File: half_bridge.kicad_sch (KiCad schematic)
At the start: 31 parts, among them Q1 IGC019S06S1XTMA1, Q2 IGC019S06S1XTMA1, U19 NCS2220AMUT1G, U4 ACS37030LLZATR-065B3, U5 LMG1205YFXR

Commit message: wip gate driver change
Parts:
- removed C21: 0402B104K6R3CT, Capacitor_SMD:C_0402_1005Metric, symbol Device:C
- removed R13, R18: ~, Resistor_SMD:R_0402_1005Metric_Pad0.72x0.64mm_HandSolder, symbol Device:R
- removed R47: CSR0402FKR500, Resistor_SMD:R_0402_1005Metric, symbol Device:R
- removed U5: LMG1205YFXR, NanoGaN:BGA12C40P4X4_173X188X68, symbol NanoGaN:LMG1205YFXR
- added C31: 0402B104K6R3CT, Capacitor_SMD:C_0402_1005Metric, symbol Device:C
- added D7: MBR2H200SF, Diode_SMD:D_SOD-123F, symbol Device:D
- added R45: 0402WGF4702TCE, Resistor_SMD:R_0402_1005Metric, symbol Device:R
- added U11, U5: 1EDN7136U, NanoGaN:1EDN71X6U, symbol NanoGaN:1EDN7116U
- C22: value 0402B104K6R3CT -> CL05B105KQ5NQNC; Capacitance 100n -> 1u; LCSC C424821 -> C307427
- R44: value CSR0402FKR500 -> 0402WGF4702TCE; LCSC C346785 -> C25792; Resistance 0R5 -> 47k
- R8, R9: value CRCW04021R00FKEDHP -> 0402WGF4702TCE; LCSC C2077491 -> C25792; Resistance 1 -> 47k
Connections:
- net HOH is gone; now on net GATE+: R8.1
- net HOL is gone; now on net GATE-: R44.1
- net LOH is gone; now on net GATE-: R9.1
- net +5V: now also U11.1 (VDD); no longer C22.1
- net GATE+: now also R45.1
- net GND: now also U11.4 (VSS); no longer C22.2
- net HIGH_GATE: now also U5.6 (OUT_SNK), U5.7 (OUT_SRC); no longer R44.2, R8.2
- net HS: now also C22.1, C31.1, U5.4 (VSS)
- net LOW_GATE: now also U11.6 (OUT_SNK), U11.7 (OUT_SRC); no longer R9.2
- new net: C22.2, C31.2, D7.1 (K)
- new net BST: D7.2 (A), U11.5 (BST), U5.1 (VDD)
- new net H+: R8.2, U5.2 (IN+)
- new net H-: R9.2, U5.3 (IN-)
- new net L+: R44.2, U11.2 (IN+)
- new net L-: R45.2, U11.3 (IN-)
- no-connect marks 0 -> 1
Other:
- note added: "Halfbridge and GateDrivers"
- note added: "U_DC High Frequency Decoupling Capacitors"
- note removed: "Gate Driver"
- note removed: "Halfbridge"
- note removed: "Q_g = 13nC Q_rr = 0 nC CBST > 5-6 nF"
- moved on the sheet: C15, C16, C20, C24, C25, C28, C36, C44, C46, C47, Q1, Q2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

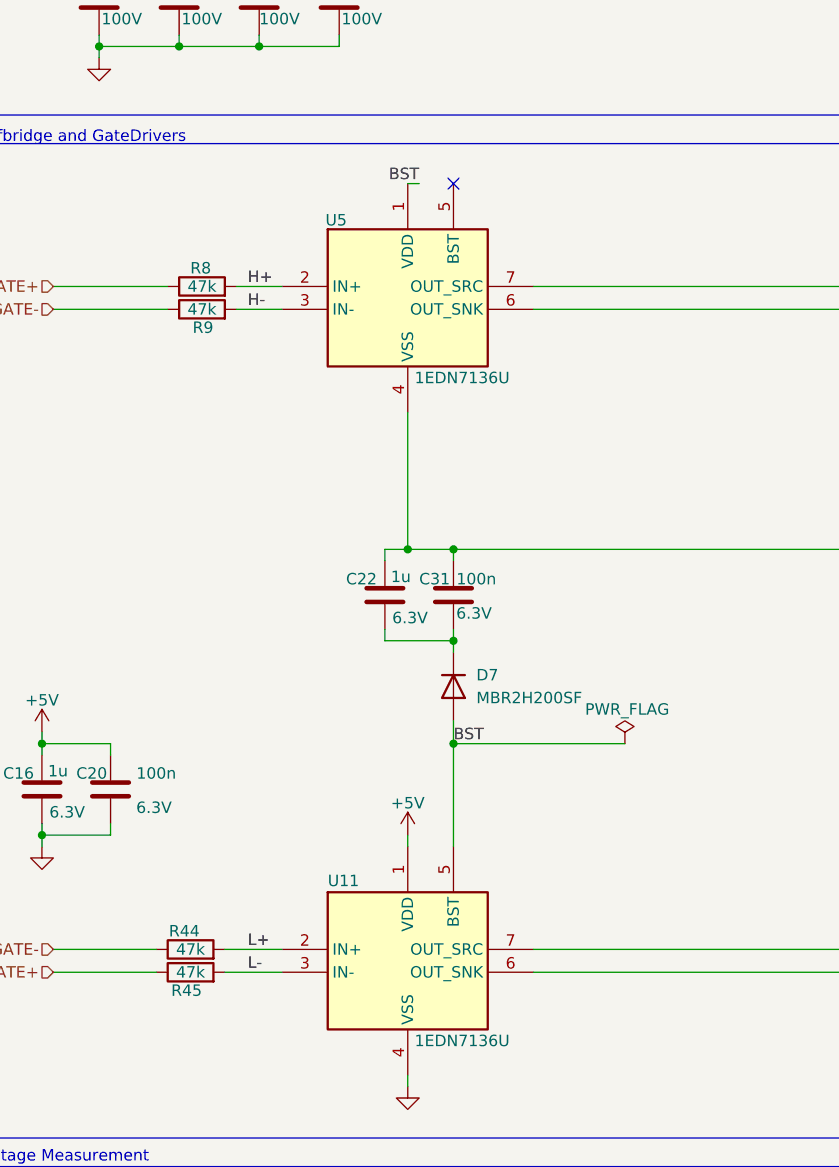
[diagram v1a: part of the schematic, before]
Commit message: gate driver change is complete
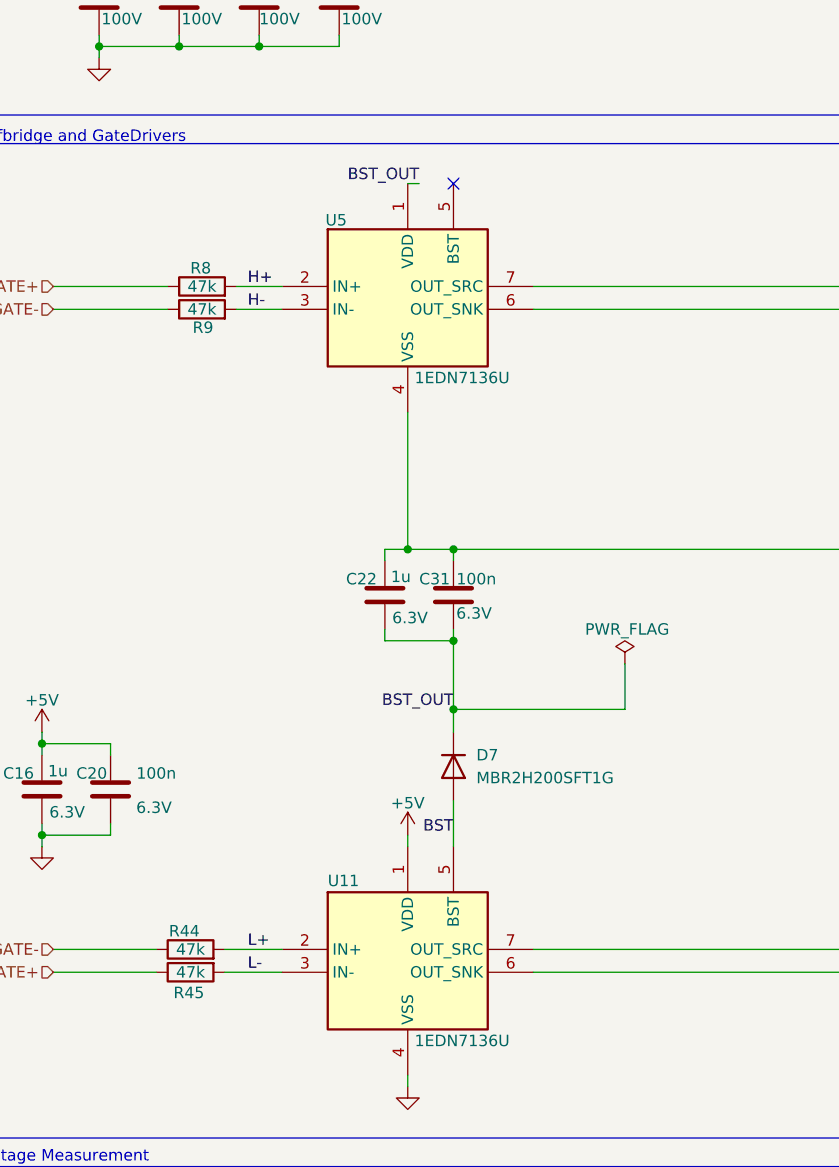
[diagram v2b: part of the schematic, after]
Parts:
- D7: value MBR2H200SF -> MBR2H200SFT1G
- R10: value 0603WAF3902T5E -> NQ02WGF3902TCE; footprint Resistor_SMD:R_0603_1608Metric -> Resistor_SMD:R_0402_1005Metric; LCSC C23153 -> C965259
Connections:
- net BST: no longer U5.1 (VDD)
- net BST_OUT: now reaches C22.2, C31.2, D7.1 (K)
- net BST_OUT: now also U5.1 (VDD)
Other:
- moved on the sheet: D7
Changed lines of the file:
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@@
 	)
 	(junction
-		(at 66.04 111.76)
-		(diameter 0)
-		(color 0 0 0 0)
-	)
-	(junction
 		(at 123.19 90.17)
 		(diameter 0)
@@
 	)
 	(junction
+		(at 66.04 107.95)
+		(diameter 0)
+		(color 0 0 0 0)
+	)
+	(junction
 		(at 20.32 111.76)
 		(diameter 0)
@@
 	)
 	(junction
+		(at 66.04 100.33)
+		(diameter 0)
+		(color 0 0 0 0)
+	)
+	(junction
 		(at 110.49 134.62)
 		(diameter 0)
@@
 	)
 	(junction
-		(at 66.04 100.33)
-		(diameter 0)
-		(color 0 0 0 0)
-	)
-	(junction
 		(at 146.05 96.52)
 		(diameter 0)
@@
 	(wire
 		(pts
-			(xy 66.04 100.33) (xy 66.04 101.6)
+			(xy 60.96 90.17) (xy 60.96 74.93)
 		)
 		(stroke
@@
 	(wire
 		(pts
-			(xy 60.96 90.17) (xy 60.96 74.93)
+			(xy 20.32 111.76) (xy 27.94 111.76)
 		)
 		(stroke
@@
 	(wire
 		(pts
-			(xy 20.32 111.76) (xy 27.94 111.76)
+			(xy 66.04 90.17) (xy 66.04 91.44)
 		)
 		(stroke
@@
 	(wire
 		(pts
-			(xy 66.04 90.17) (xy 66.04 91.44)
+			(xy 58.42 100.33) (xy 66.04 100.33)
 		)
 		(stroke
@@
 	(wire
 		(pts
-			(xy 66.04 111.76) (xy 66.04 123.19)
-		)
-		(stroke
-			(width 0)
-			(type default)
-		)
-	)
-	(wire
-		(pts
 			(xy 243.84 118.11) (xy 237.49 118.11)
 		)
@@
 	(wire
 		(pts
-			(xy 66.04 109.22) (xy 66.04 111.76)
-		)
-		(stroke
-			(width 0)
-			(type default)
-		)
-	)
-	(wire
-		(pts
 			(xy 60.96 49.53) (xy 62.23 49.53)
 		)
@@
 	(wire
 		(pts
+			(xy 85.09 107.95) (xy 85.09 102.87)
+		)
+		(stroke
+			(width 0)
+			(type default)
+		)
+	)
+	(wire
+		(pts
 			(xy 152.4 129.54) (xy 153.67 129.54)
 		)
@@
 	(wire
 		(pts
-			(xy 21.59 137.16) (xy 33.02 137.16)
-		)
-		(stroke
-			(width 0)
-			(type default)
-		)
-	)
-	(wire
-		(pts
-			(xy 66.04 100.33) (xy 58.42 100.33)
-		)
-		(stroke
-			(width 0)
-			(type default)
-		)
-	)
-	(wire
-		(pts
 			(xy 19.05 187.96) (xy 19.05 189.23)
 		)
@@
 	(wire
 		(pts
+			(xy 66.04 100.33) (xy 66.04 107.95)
+		)
+		(stroke
+			(width 0)
+			(type default)
+		)
+	)
+	(wire
+		(pts
 			(xy 227.33 96.52) (xy 227.33 106.68)
 		)
@@
 	(wire
 		(pts
+			(xy 66.04 118.11) (xy 66.04 123.19)
+		)
+		(stroke
+			(width 0)
+			(type default)
+		)
+	)
+	(wire
+		(pts
 			(xy 227.33 96.52) (xy 266.7 96.52)
 		)
@@
 	(wire
 		(pts
-			(xy 40.64 137.16) (xy 46.99 137.16)
+			(xy 85.09 107.95) (xy 66.04 107.95)
 		)
 		(stroke
@@
 	(wire
 		(pts
-			(xy 85.09 111.76) (xy 66.04 111.76)
+			(xy 180.34 128.27) (xy 180.34 125.73)
 		)
 		(stroke
@@
 	(wire
 		(pts
-			(xy 180.34 128.27) (xy 180.34 125.73)
+			(xy 243.84 142.24) (xy 237.49 142.24)
 		)
 		(stroke
@@
 	(wire
 		(pts
-			(xy 243.84 142.24) (xy 237.49 142.24)
+			(xy 20.32 121.92) (xy 27.94 121.92)
 		)
 		(stroke
@@
 	(wire
 		(pts
-			(xy 20.32 121.92) (xy 27.94 121.92)
+			(xy 19.05 175.26) (xy 30.48 175.26)
 		)
 		(stroke
@@
 	(wire
 		(pts
-			(xy 19.05 175.26) (xy 30.48 175.26)
+			(xy 19.05 175.26) (xy 19.05 177.8)
 		)
 		(stroke
@@
 	(wire
 		(pts
-			(xy 19.05 175.26) (xy 19.05 177.8)
+			(xy 74.93 63.5) (xy 110.49 63.5)
 		)
 		(stroke
@@
 	(wire
 		(pts
-			(xy 74.93 63.5) (xy 110.49 63.5)
+			(xy 237.49 135.89) (xy 236.22 135.89)
 		)
 		(stroke
@@
 	(wire
 		(pts
-			(xy 237.49 135.89) (xy 236.22 135.89)
+			(xy 21.59 137.16) (xy 33.02 137.16)
 		)
 		(stroke
@@
 	(wire
 		(pts
+			(xy 66.04 110.49) (xy 66.04 107.95)
+		)
+		(stroke
+			(width 0)
+			(type default)
+		)
+	)
+	(wire
+		(pts
 			(xy 227.33 106.68) (xy 237.49 106.68)
 		)
@@
 	(wire
 		(pts
+			(xy 40.64 137.16) (xy 46.99 137.16)
+		)
+		(stroke
+			(width 0)
+			(type default)
+		)
+	)
+	(wire
+		(pts
 			(xy 220.98 111.76) (xy 228.6 111.76)
 		)
@@
 		)
 	)
-	(label "L-"
-		(at 43.18 137.16 0)
+	(label "BST_OUT"
+		(at 66.04 107.95 180)
 		(effects
 			(font
 				(size 1.27 1.27)
 			)
-			(justify left bottom)
+			(justify right bottom)
 		)
 	)
-	(label "H-"
-		(at 43.18 63.5 0)
+	(label "L-"
+		(at 43.18 137.16 0)
 		(effects
 			(font
@@
 		)
 	)
-	(label "LOW_GATE"
-		(at 109.22 134.62 0)
+	(label "H-"
+		(at 43.18 63.5 0)
 		(effects
 			(font
@@
 	)
 	(label "BST"
-		(at 62.23 49.53 180)
+		(at 66.04 121.92 180)
 		(effects
 			(font
@@
 		)
 	)
-	(label "BST"
-		(at 66.04 111.76 0)
+	(label "LOW_GATE"
+		(at 109.22 134.62 0)
 		(effects
 			(font
@@
 		)
 	)
+	(label "BST_OUT"
+		(at 62.23 49.53 180)
+		(effects
+			(font
+				(size 1.27 1.27)
+			)
+			(justify right bottom)
+		)
+	)
 	(label "L+"
 		(at 43.18 134.62 0)
@@
 	(symbol
 		(lib_id "Device:D")
-		(at 66.04 105.41 270)
+		(at 66.04 114.3 270)
 		(unit 1)
 		(exclude_from_sim no)
@@
 		(on_board yes)
 		(dnp no)
-		(fields_autoplaced yes)
 		(property "Reference" "D7"
-			(at 68.58 104.1399 90)
+			(at 68.58 113.0299 90)
 			(effects
 				(font
@@
 			)
 		)
-		(property "Value" "MBR2H200SF"
-			(at 68.58 106.6799 90)
+		(property "Value" "MBR2H200SFT1G"
+			(at 68.58 115.5699 90)
 			(effects
 				(font
@@
 		)
 		(property "Footprint" "Diode_SMD:D_SOD-123F"
-			(at 66.04 105.41 0)
+			(at 66.04 114.3 0)
 			(effects
 				(font
@@
 		)
 		(property "Datasheet" "https://www.onsemi.com/pdf/datasheet/mbr2h200sf-d.pdf"
-			(at 66.04 105.41 0)
+			(at 66.04 114.3 0)
 			(effects
 				(font
@@
 		)
 		(property "Description" "-55℃~+150℃ 1 Independent 200V 200uA@200V 2A 30A 940mV@2A SOD-123 Schottky Diodes ROHS"
-			(at 66.04 105.41 0)
+			(at 66.04 114.3 0)
 			(effects
 				(font
@@
 		)
 		(property "LCSC" "C480689"
-			(at 66.04 105.41 90)
+			(at 66.04 114.3 90)
 			(effects
 				(font
@@
 		(lib_id "Device:R")
 		(at 36.83 137.16 90)
+		(mirror x)
 		(unit 1)
 		(exclude_from_sim no)
@@
 		(dnp no)
 		(property "Reference" "R45"
-			(at 38.1 139.192 90)
+			(at 38.354 139.446 90)
 			(effects
 				(font
@@
 		)
 		(property "Value" "0402WGF4702TCE"
-			(at 38.0999 134.62 0)
+			(at 38.0999 139.7 0)
 			(effects
 				(font
@@
 		)
 		(property "Footprint" "Resistor_SMD:R_0402_1005Metric"
-			(at 36.83 138.938 90)
+			(at 36.83 135.382 90)
 			(effects
 				(font
@@
 	(symbol
 		(lib_id "power:PWR_FLAG")
-		(at 85.09 111.76 0)
+		(at 85.09 102.87 0)
 		(unit 1)
 		(exclude_from_sim no)
@@
 		(dnp no)
 		(property "Reference" "#FLG04"
-			(at 85.09 109.855 0)
+			(at 85.09 100.965 0)
 			(effects
 				(font
@@
 		)
 		(property "Value" "PWR_FLAG"
-			(at 85.344 107.95 0)
+			(at 85.344 99.06 0)
 			(effects
 				(font
@@
 		)
 		(property "Footprint" ""
-			(at 85.09 111.76 0)
+			(at 85.09 102.87 0)
 			(effects
 				(font
@@
 		)
 		(property "Datasheet" "~"
-			(at 85.09 111.76 0)
+			(at 85.09 102.87 0)
 			(effects
 				(font
@@
 		)
 		(property "Description" ""
-			(at 85.09 111.76 0)
+			(at 85.09 102.87 0)
 			(effects
 				(font
@@
 			)
 		)
-		(property "Value" "0603WAF3902T5E"
+		(property "Value" "NQ02WGF3902TCE"
 			(at 21.59 170.1799 0)
 			(effects
@@
 			)
 		)
-		(property "Footprint" "Resistor_SMD:R_0603_1608Metric"
+		(property "Footprint" "Resistor_SMD:R_0402_1005Metric"
 			(at 17.272 168.91 90)
 			(effects
@@
 			)
 		)
-		(property "LCSC" "C23153"
+		(property "LCSC" "C965259"
 			(at 19.05 168.91 0)
 			(effects

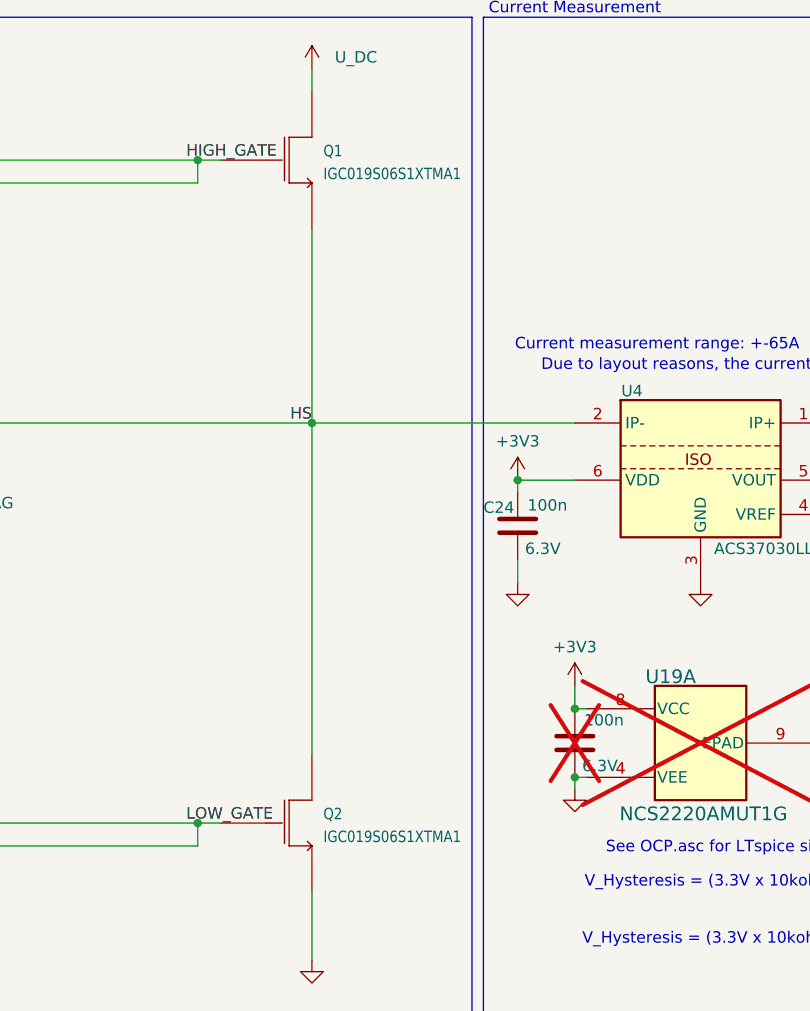
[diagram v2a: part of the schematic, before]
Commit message: small order changes and ESD warning symbol
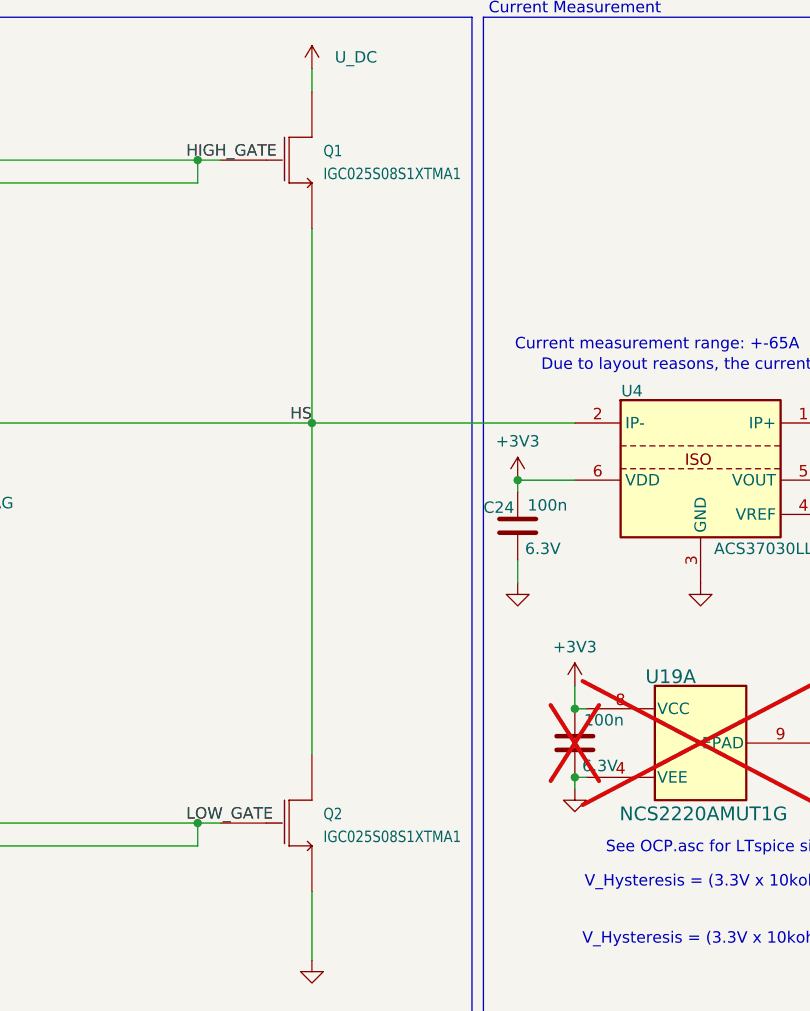
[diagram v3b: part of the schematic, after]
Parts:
- Q1, Q2: value IGC019S06S1XTMA1 -> IGC025S08S1XTMA1; LCSC C43313313 -> C43313314
- U11, U5: LCSC C3654881 -> C5484766
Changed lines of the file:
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@@
 			)
 		)
-		(property "Value" "IGC019S06S1XTMA1"
+		(property "Value" "IGC025S08S1XTMA1"
 			(at 124.46 62.4839 0)
 			(effects
@@
 			)
 		)
-		(property "Description" "CoolGaN™ Transistor 60 V G3 in PQFN 3x5, 1.9 mΩ"
+		(property "Description" "CoolGaN™ Transistor 80 V G3 in PQFN 3x5, 1.9 mΩ"
 			(at 122.936 46.99 0)
 			(effects
@@
 			)
 		)
-		(property "LCSC" "C43313313"
+		(property "LCSC" "C43313314"
 			(at 118.11 58.42 0)
 			(effects
@@
 			)
 		)
-		(property "LCSC" "C3654881"
+		(property "LCSC" "C5484766"
 			(at 39.116 157.988 0)
 			(effects
@@
 			)
 		)
-		(property "LCSC" "C3654881"
+		(property "LCSC" "C5484766"
 			(at 39.116 84.328 0)
 			(effects
@@
 			)
 		)
-		(property "Value" "IGC019S06S1XTMA1"
+		(property "Value" "IGC025S08S1XTMA1"
 			(at 124.46 136.1439 0)
 			(effects
@@
 			)
 		)
-		(property "Description" "CoolGaN™ Transistor 60 V G3 in PQFN 3x5, 1.9 mΩ"
+		(property "Description" "CoolGaN™ Transistor 80 V G3 in PQFN 3x5, 1.9 mΩ"
 			(at 122.936 120.65 0)
 			(effects
@@
 			)
 		)
-		(property "LCSC" "C43313313"
+		(property "LCSC" "C43313314"
 			(at 118.11 132.08 0)
 			(effects
